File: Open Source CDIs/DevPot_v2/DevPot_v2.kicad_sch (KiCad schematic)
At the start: 21 parts, among them J1 COIL, J2 MAG, J3 GtD, J4 AtG, J5 scrD, J6 lD, J7 aD, J8 aC, Q1 TIC106

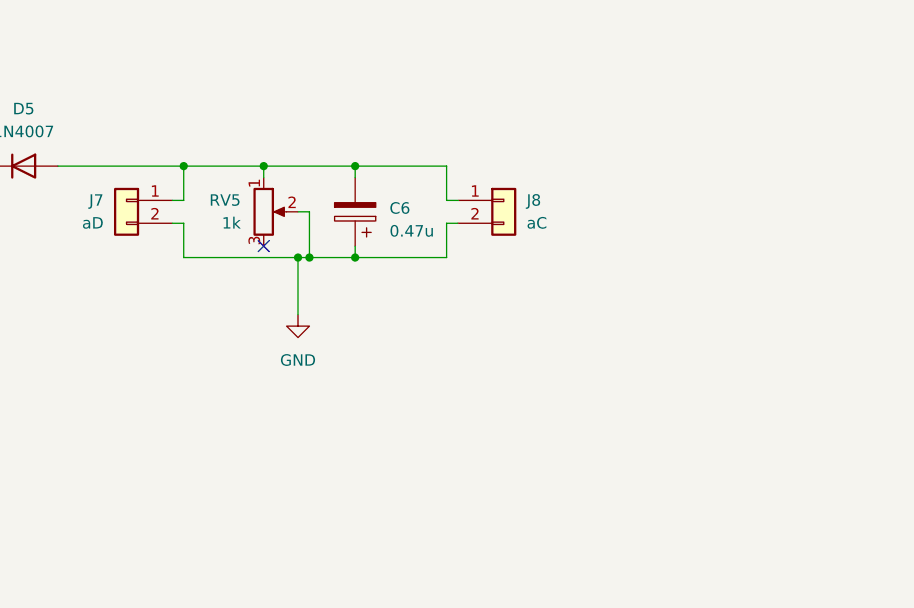
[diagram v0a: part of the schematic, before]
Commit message: Added new CDIs and updated README
Added the DevPot_v2 CDI, updated the readme to include all of the new CDIs and included images for each. Also add production exports for all the boards.
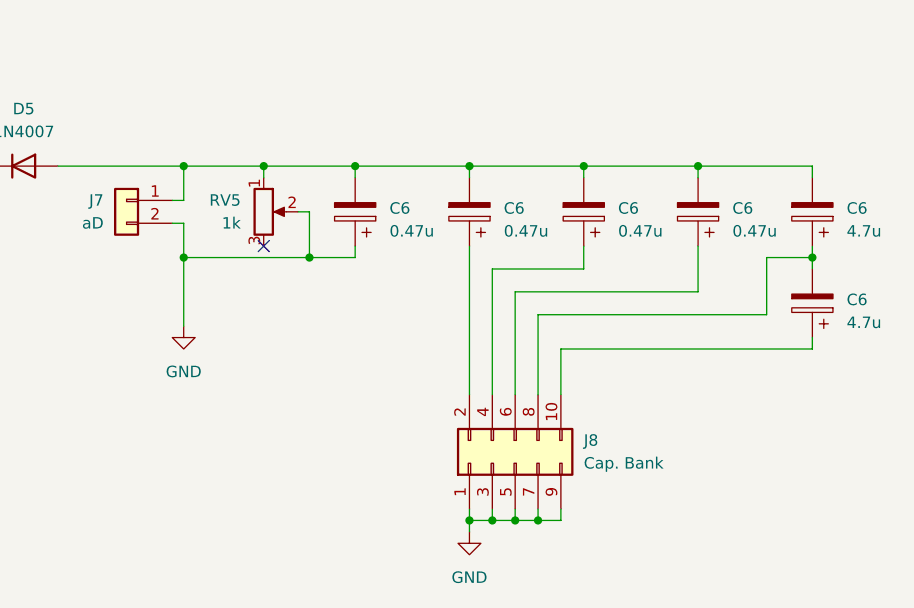
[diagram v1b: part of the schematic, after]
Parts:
- removed J8: aC, TE_1792863:TE_1792863, symbol Connector_Generic:Conn_01x02
- added C6 (x3): 0.47u, Capacitor_THT:CP_Radial_Tantal_D5.5mm_P2.50mm, symbol Device:C_Polarized
- added C6 (x2): 4.7u, Capacitor_THT:CP_Radial_Tantal_D5.5mm_P2.50mm, symbol Device:C_Polarized
- added J8: Cap. Bank, Connector_PinHeader_2.54mm:PinHeader_2x05_P2.54mm_Vertical, symbol Connector_Generic:Conn_02x05_Odd_Even
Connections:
- net GND: now also J8.1 (Pin_1), J8.3 (Pin_3), J8.5 (Pin_5), J8.7 (Pin_7), J8.9 (Pin_9)
- net at C6.2, D5.2 (A), J7.1 (Pin_1)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: now also C6.2, C6.2, C6.2, C6.2
- new net: C6.1, J8.6 (Pin_6)
- new net: C6.1, J8.10 (Pin_10)
- new net: C6.1, J8.2 (Pin_2)
- new net: C6.1, J8.4 (Pin_4)
- new net: C6.1, C6.2, J8.8 (Pin_8)
